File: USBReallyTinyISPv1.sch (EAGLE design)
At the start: 20 parts, among them IC1 ATTINY2313, IC2 74AC125D, Q1 12 MHz, X1 miniUSB-B

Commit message: Getting it ready for printing
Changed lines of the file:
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@@
 <?xml version="1.0" encoding="utf-8"?>
 <!DOCTYPE eagle SYSTEM "eagle.dtd">
-<eagle version="6.1">
+<eagle version="7.4.0">
 <drawing>
 <settings>
@@
 <segment>
 <pinref part="IC1" gate="G$1" pin="(T0)PD4"/>
-<wire x1="99.06" y1="71.12" x2="116.84" y2="71.12" width="0.1524" layer="91"/>
-<wire x1="116.84" y1="71.12" x2="116.84" y2="119.38" width="0.1524" layer="91"/>
+<wire x1="99.06" y1="71.12" x2="114.3" y2="71.12" width="0.1524" layer="91"/>
+<wire x1="114.3" y1="71.12" x2="114.3" y2="119.38" width="0.1524" layer="91"/>
 <pinref part="IC2" gate="D" pin="OE"/>
-<wire x1="116.84" y1="119.38" x2="101.6" y2="119.38" width="0.1524" layer="91"/>
+<wire x1="114.3" y1="119.38" x2="101.6" y2="119.38" width="0.1524" layer="91"/>
 <pinref part="IC2" gate="C" pin="OE"/>
-<wire x1="116.84" y1="119.38" x2="134.62" y2="119.38" width="0.1524" layer="91"/>
+<wire x1="114.3" y1="119.38" x2="134.62" y2="119.38" width="0.1524" layer="91"/>
 <wire x1="134.62" y1="119.38" x2="134.62" y2="121.92" width="0.1524" layer="91"/>
 <pinref part="IC2" gate="B" pin="OE"/>
@@
 <junction x="134.62" y="121.92"/>
 <junction x="134.62" y="139.7"/>
-<junction x="116.84" y="119.38"/>
-</segment>
-</net>
+<junction x="114.3" y="119.38"/>
+</segment>
+</net>

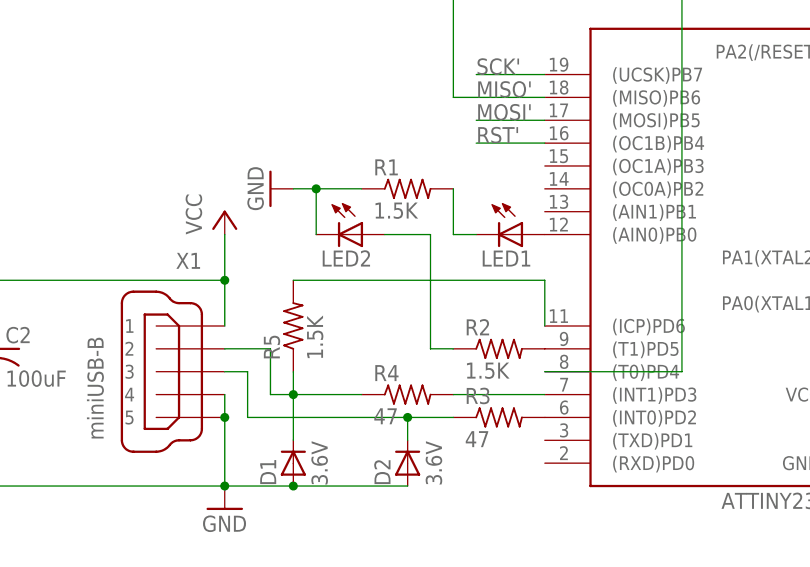
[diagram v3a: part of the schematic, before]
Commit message: Changed size of 1.5kOhm resistors
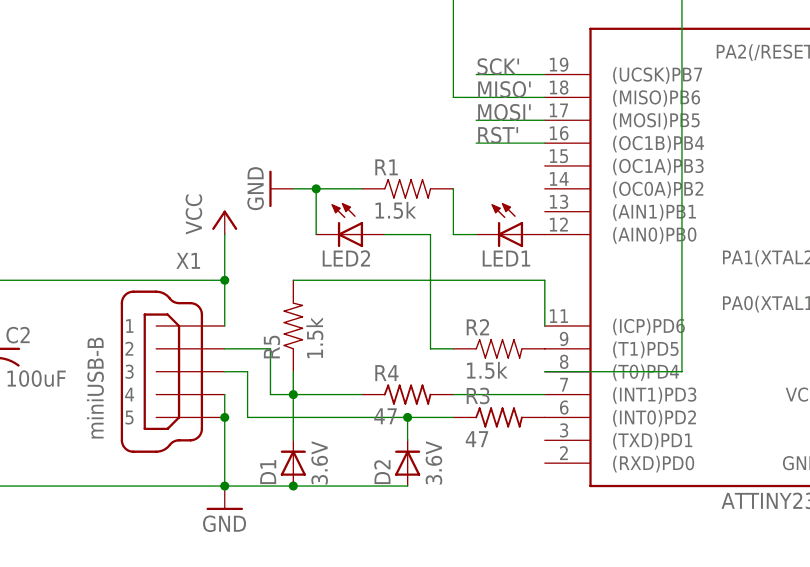
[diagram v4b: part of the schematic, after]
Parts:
- R1, R2, R5: value 1.5K -> 1.5k; device resistor:R-US_R0805 -> SparkFun-Resistors:RESISTOR1206
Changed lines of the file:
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@@
 <layer number="223" name="223bmp" color="24" fill="1" visible="no" active="no"/>
 <layer number="224" name="224bmp" color="25" fill="1" visible="no" active="no"/>
+<layer number="225" name="225bmp" color="7" fill="1" visible="yes" active="yes"/>
+<layer number="226" name="226bmp" color="7" fill="1" visible="yes" active="yes"/>
+<layer number="227" name="227bmp" color="7" fill="1" visible="yes" active="yes"/>
+<layer number="228" name="228bmp" color="7" fill="1" visible="yes" active="yes"/>
+<layer number="229" name="229bmp" color="7" fill="1" visible="yes" active="yes"/>
+<layer number="230" name="230bmp" color="7" fill="1" visible="yes" active="yes"/>
 <layer number="231" name="Eagle3D_PG1" color="7" fill="1" visible="no" active="no"/>
 <layer number="232" name="Eagle3D_PG2" color="7" fill="1" visible="no" active="no"/>
@@
 <part name="IC2" library="74xx-eu" deviceset="74*125" device="D" technology="AC"/>
 <part name="Q1" library="murata-filter" deviceset="CSTCR" device="" technology="6M00G53Z" value="12 MHz"/>
-<part name="R1" library="resistor" deviceset="R-US_" device="R0805" value="1.5K"/>
-<part name="R2" library="resistor" deviceset="R-US_" device="R0805" value="1.5K"/>
 <part name="R3" library="resistor" deviceset="R-US_" device="R0805" value="47"/>
 <part name="R4" library="resistor" deviceset="R-US_" device="R0805" value="47"/>
-<part name="R5" library="resistor" deviceset="R-US_" device="R0805" value="1.5K"/>
 <part name="R6" library="resistor" deviceset="R-US_" device="R0805" value="10K"/>
 <part name="IC1" library="avr-7" deviceset="TINY2313*" device="-*S*" value="ATTINY2313"/>
@@
 <part name="GND5" library="supply1" deviceset="GND" device=""/>
 <part name="JP1" library="adafruit" deviceset="PINHD-1X3" device=""/>
+<part name="R1" library="SparkFun-Resistors" deviceset="RESISTOR" device="1206" value="1.5k"/>
+<part name="R2" library="SparkFun-Resistors" deviceset="RESISTOR" device="1206" value="1.5k"/>
+<part name="R5" library="SparkFun-Resistors" deviceset="RESISTOR" device="1206" value="1.5k"/>
 </parts>
 <sheets>
@@
 </instance>
 <instance part="Q1" gate="G$1" x="144.78" y="81.28" rot="R90"/>
-<instance part="R1" gate="G$1" x="83.82" y="91.44"/>
-<instance part="R2" gate="G$1" x="93.98" y="73.66"/>
 <instance part="R3" gate="G$1" x="93.98" y="66.04"/>
 <instance part="R4" gate="G$1" x="83.82" y="68.58"/>
-<instance part="R5" gate="G$1" x="71.12" y="76.2" rot="R90"/>
 <instance part="R6" gate="G$1" x="142.24" y="106.68"/>
 <instance part="IC1" gate="G$1" x="116.84" y="88.9" rot="MR0"/>
@@
 <instance part="GND5" gate="1" x="71.12" y="134.62"/>
 <instance part="JP1" gate="A" x="81.28" y="152.4" rot="R90"/>
+<instance part="R1" gate="G$1" x="83.82" y="91.44"/>
+<instance part="R2" gate="G$1" x="93.98" y="73.66"/>
+<instance part="R5" gate="G$1" x="71.12" y="76.2" rot="R90"/>
 </instances>
 <busses>
@@
 </segment>
 <segment>
-<pinref part="R1" gate="G$1" pin="1"/>
 <pinref part="GND3" gate="1" pin="GND"/>
 <wire x1="78.74" y1="91.44" x2="73.66" y2="91.44" width="0.1524" layer="91"/>
@@
 <wire x1="73.66" y1="86.36" x2="73.66" y2="91.44" width="0.1524" layer="91"/>
 <junction x="73.66" y="91.44"/>
+<pinref part="R1" gate="G$1" pin="1"/>
 </segment>
 <segment>
@@
 </segment>
 </net>
-<net name="N$5" class="0">
-<segment>
-<pinref part="IC1" gate="G$1" pin="(T1)PD5"/>
-<pinref part="R2" gate="G$1" pin="2"/>
-</segment>
-</net>
 <net name="N$6" class="0">
 <segment>
 <wire x1="81.28" y1="86.36" x2="86.36" y2="86.36" width="0.1524" layer="91"/>
 <wire x1="86.36" y1="86.36" x2="86.36" y2="73.66" width="0.1524" layer="91"/>
-<pinref part="R2" gate="G$1" pin="1"/>
 <wire x1="86.36" y1="73.66" x2="88.9" y2="73.66" width="0.1524" layer="91"/>
 <pinref part="LED2" gate="G$1" pin="A"/>
+<pinref part="R2" gate="G$1" pin="1"/>
 </segment>
 </net>
 <net name="N$7" class="0">
 <segment>
-<pinref part="R1" gate="G$1" pin="2"/>
 <wire x1="88.9" y1="86.36" x2="88.9" y2="91.44" width="0.1524" layer="91"/>
 <pinref part="LED1" gate="G$1" pin="C"/>
 <wire x1="91.44" y1="86.36" x2="88.9" y2="86.36" width="0.1524" layer="91"/>
+<pinref part="R1" gate="G$1" pin="2"/>
 </segment>
 </net>
@@
 <wire x1="71.12" y1="63.5" x2="71.12" y2="68.58" width="0.1524" layer="91"/>
 <junction x="71.12" y="68.58"/>
-<pinref part="R5" gate="G$1" pin="1"/>
 <wire x1="71.12" y1="68.58" x2="71.12" y2="71.12" width="0.1524" layer="91"/>
 <pinref part="D1" gate="G$1" pin="K"/>
+<pinref part="R5" gate="G$1" pin="1"/>
 </segment>
 </net>
@@
 <segment>
 <pinref part="IC1" gate="G$1" pin="(ICP)PD6"/>
-<pinref part="R5" gate="G$1" pin="2"/>
 <wire x1="99.06" y1="76.2" x2="99.06" y2="81.28" width="0.1524" layer="91"/>
 <wire x1="99.06" y1="81.28" x2="71.12" y2="81.28" width="0.1524" layer="91"/>
+<pinref part="R5" gate="G$1" pin="2"/>
 </segment>
 </net>
@@
 </segment>
 </net>
+<net name="N$5" class="0">
+<segment>
+<pinref part="IC1" gate="G$1" pin="(T1)PD5"/>
+<pinref part="R2" gate="G$1" pin="2"/>
+</segment>
+</net>

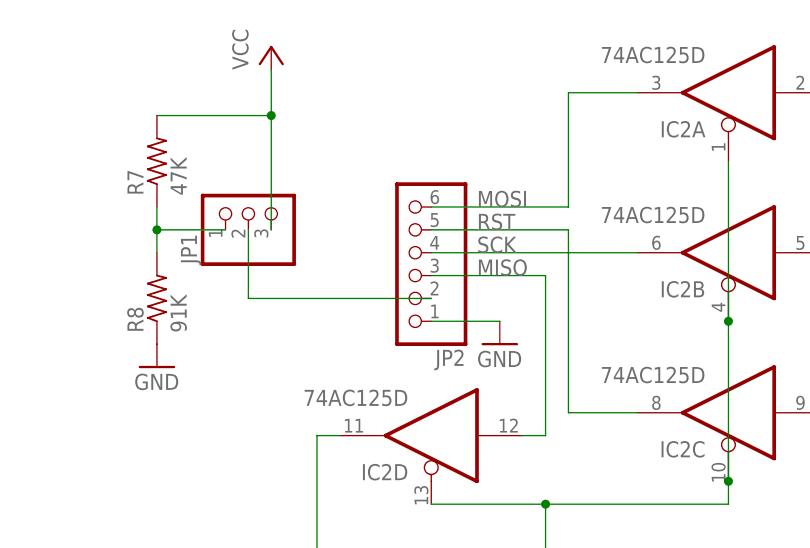
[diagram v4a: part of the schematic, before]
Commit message: Updated headers to have bigger pads
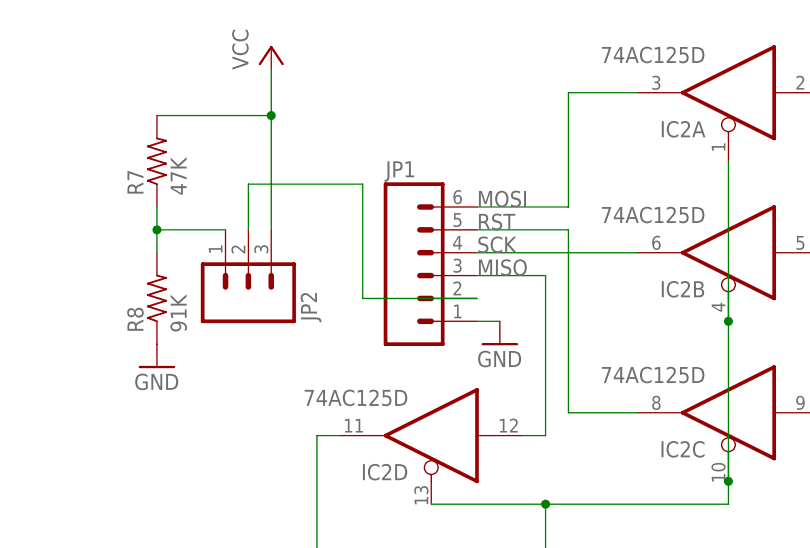
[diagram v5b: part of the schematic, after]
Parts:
- JP1: device adafruit:PINHD-1X3 -> SparkFun-Connectors:M06SILK_FEMALE_PTH
- JP2: device adafruit:PINHD-1X6 -> mine:M03-SHORTEDPTH
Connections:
- net GND: now also JP1.1; no longer JP2.1
- net MISO: now also JP1.3; no longer JP2.3
- net MOSI: now also JP1.6; no longer JP2.6
- net N$15: now also JP2.1; no longer JP1.1
- net RST: now also JP1.5; no longer JP2.5
- net SCK: now also JP1.4; no longer JP2.4
- net VCC: now also JP2.3; no longer JP1.3
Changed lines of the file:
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@@
 <?xml version="1.0" encoding="utf-8"?>
 <!DOCTYPE eagle SYSTEM "eagle.dtd">
-<eagle version="7.4.0">
+<eagle version="6.6.0">
 <drawing>
 <settings>
@@
 <layer number="56" name="wert" color="7" fill="1" visible="no" active="no"/>
 <layer number="57" name="tCAD" color="7" fill="1" visible="no" active="no"/>
+<layer number="59" name="tCarbon" color="7" fill="1" visible="no" active="no"/>
+<layer number="60" name="bCarbon" color="7" fill="1" visible="no" active="no"/>
 <layer number="90" name="Modules" color="7" fill="1" visible="no" active="yes"/>
 <layer number="91" name="Nets" color="2" fill="1" visible="yes" active="yes"/>
@@
 <layer number="112" name="tSilk" color="7" fill="1" visible="yes" active="yes"/>
 <layer number="113" name="ReferenceLS" color="7" fill="1" visible="no" active="no"/>
+<layer number="114" name="Badge_Outline" color="7" fill="1" visible="yes" active="yes"/>
+<layer number="115" name="ReferenceISLANDS" color="7" fill="1" visible="yes" active="yes"/>
 <layer number="116" name="Patch_BOT" color="9" fill="4" visible="yes" active="yes"/>
 <layer number="118" name="Rect_Pads" color="7" fill="1" visible="no" active="no"/>
@@
 <layer number="127" name="_tValues" color="7" fill="1" visible="yes" active="yes"/>
 <layer number="128" name="_bValues" color="7" fill="1" visible="yes" active="yes"/>
+<layer number="129" name="Mask" color="7" fill="1" visible="yes" active="yes"/>
 <layer number="131" name="tAdjust" color="7" fill="1" visible="no" active="yes"/>
 <layer number="132" name="bAdjust" color="7" fill="1" visible="no" active="yes"/>
@@
 <layer number="251" name="SMDround" color="7" fill="1" visible="no" active="no"/>
 <layer number="254" name="cooling" color="7" fill="1" visible="yes" active="yes"/>
+<layer number="255" name="routoute" color="7" fill="1" visible="yes" active="yes"/>
 </layers>
 <schematic xreflabel="%F%N/%S.%C%R" xrefpart="/%S.%C%R">
@@
 <part name="D1" library="ipc-7351-diode" deviceset="DIODE_" device="SOD-123" value="3.6V"/>
 <part name="D2" library="ipc-7351-diode" deviceset="DIODE_" device="SOD-123" value="3.6V"/>
-<part name="JP2" library="adafruit" deviceset="PINHD-1X6" device=""/>
 <part name="GND6" library="supply1" deviceset="GND" device=""/>
 <part name="R7" library="resistor" deviceset="R-US_" device="R0805" value="47K"/>
 <part name="R8" library="resistor" deviceset="R-US_" device="R0805" value="91K"/>
 <part name="GND5" library="supply1" deviceset="GND" device=""/>
-<part name="JP1" library="adafruit" deviceset="PINHD-1X3" device=""/>
 <part name="R1" library="SparkFun-Resistors" deviceset="RESISTOR" device="1206" value="1.5k"/>
 <part name="R2" library="SparkFun-Resistors" deviceset="RESISTOR" device="1206" value="1.5k"/>
 <part name="R5" library="SparkFun-Resistors" deviceset="RESISTOR" device="1206" value="1.5k"/>
+<part name="JP1" library="SparkFun-Connectors" deviceset="M06" device="SILK_FEMALE_PTH"/>
+<part name="JP2" library="mine" deviceset="M03-SHORTED" device="PTH"/>
 </parts>
 <sheets>
@@
 <instance part="D1" gate="G$1" x="71.12" y="60.96" rot="R90"/>
 <instance part="D2" gate="G$1" x="83.82" y="60.96" rot="R90"/>
-<instance part="JP2" gate="A" x="99.06" y="147.32" rot="R180"/>
 <instance part="GND6" gate="1" x="109.22" y="137.16"/>
 <instance part="R7" gate="G$1" x="71.12" y="157.48" rot="R90"/>
 <instance part="R8" gate="G$1" x="71.12" y="142.24" rot="R90"/>
 <instance part="GND5" gate="1" x="71.12" y="134.62"/>
-<instance part="JP1" gate="A" x="81.28" y="152.4" rot="R90"/>
 <instance part="R1" gate="G$1" x="83.82" y="91.44"/>
 <instance part="R2" gate="G$1" x="93.98" y="73.66"/>
 <instance part="R5" gate="G$1" x="71.12" y="76.2" rot="R90"/>
+<instance part="JP1" gate="G$1" x="101.6" y="144.78"/>
+<instance part="JP2" gate="G$1" x="81.28" y="142.24" rot="MR90"/>
 </instances>
 <busses>
@@
 </segment>
 <segment>
-<pinref part="JP2" gate="A" pin="1"/>
 <pinref part="GND6" gate="1" pin="GND"/>
-<wire x1="101.6" y1="139.7" x2="109.22" y2="139.7" width="0.1524" layer="91"/>
+<wire x1="106.68" y1="139.7" x2="109.22" y2="139.7" width="0.1524" layer="91"/>
+<pinref part="JP1" gate="G$1" pin="1"/>
 </segment>
 <segment>
@@
 <wire x1="71.12" y1="162.56" x2="83.82" y2="162.56" width="0.1524" layer="91"/>
 <junction x="83.82" y="162.56"/>
-<pinref part="JP1" gate="A" pin="3"/>
+<pinref part="JP2" gate="G$1" pin="3"/>
 </segment>
 </net>
@@
 <pinref part="IC2" gate="A" pin="O"/>
 <wire x1="124.46" y1="165.1" x2="116.84" y2="165.1" width="0.1524" layer="91"/>
-<pinref part="JP2" gate="A" pin="6"/>
-<wire x1="101.6" y1="152.4" x2="116.84" y2="152.4" width="0.1524" layer="91"/>
+<wire x1="106.68" y1="152.4" x2="116.84" y2="152.4" width="0.1524" layer="91"/>
 <wire x1="116.84" y1="152.4" x2="116.84" y2="165.1" width="0.1524" layer="91"/>
+<pinref part="JP1" gate="G$1" pin="6"/>
 </segment>
 </net>
@@
 <label x="106.68" y="144.78" size="1.778" layer="95"/>
 <pinref part="IC2" gate="D" pin="I"/>
-<pinref part="JP2" gate="A" pin="3"/>
 <wire x1="114.3" y1="144.78" x2="114.3" y2="127" width="0.1524" layer="91"/>
 <wire x1="114.3" y1="127" x2="111.76" y2="127" width="0.1524" layer="91"/>
-<wire x1="101.6" y1="144.78" x2="114.3" y2="144.78" width="0.1524" layer="91"/>
+<wire x1="106.68" y1="144.78" x2="114.3" y2="144.78" width="0.1524" layer="91"/>
+<pinref part="JP1" gate="G$1" pin="3"/>
 </segment>
 </net>
@@
 <label x="106.68" y="147.32" size="1.778" layer="95"/>
 <pinref part="IC2" gate="B" pin="O"/>
-<wire x1="124.46" y1="147.32" x2="101.6" y2="147.32" width="0.1524" layer="91"/>
-<pinref part="JP2" gate="A" pin="4"/>
+<wire x1="124.46" y1="147.32" x2="106.68" y2="147.32" width="0.1524" layer="91"/>
+<pinref part="JP1" gate="G$1" pin="4"/>
 </segment>
 </net>
@@
 <wire x1="116.84" y1="149.86" x2="116.84" y2="129.54" width="0.1524" layer="91"/>
 <wire x1="116.84" y1="129.54" x2="124.46" y2="129.54" width="0.1524" layer="91"/>
-<pinref part="JP2" gate="A" pin="5"/>
-<wire x1="101.6" y1="149.86" x2="116.84" y2="149.86" width="0.1524" layer="91"/>
+<wire x1="106.68" y1="149.86" x2="116.84" y2="149.86" width="0.1524" layer="91"/>
+<pinref part="JP1" gate="G$1" pin="5"/>
 </segment>
 </net>
@@
 <net name="N$13" class="0">
 <segment>
-<pinref part="JP2" gate="A" pin="2"/>
-<wire x1="101.6" y1="142.24" x2="81.28" y2="142.24" width="0.1524" layer="91"/>
-<wire x1="81.28" y1="142.24" x2="81.28" y2="149.86" width="0.1524" layer="91"/>
-<pinref part="JP1" gate="A" pin="2"/>
+<wire x1="81.28" y1="149.86" x2="81.28" y2="154.94" width="0.1524" layer="91"/>
+<wire x1="81.28" y1="154.94" x2="93.98" y2="154.94" width="0.1524" layer="91"/>
+<pinref part="JP1" gate="G$1" pin="2"/>
+<wire x1="106.68" y1="142.24" x2="93.98" y2="142.24" width="0.1524" layer="91"/>
+<wire x1="93.98" y1="142.24" x2="93.98" y2="154.94" width="0.1524" layer="91"/>
+<pinref part="JP2" gate="G$1" pin="2"/>
 </segment>
 </net>
@@
 <wire x1="78.74" y1="149.86" x2="71.12" y2="149.86" width="0.1524" layer="91"/>
 <junction x="71.12" y="149.86"/>
-<pinref part="JP1" gate="A" pin="1"/>
-</segment>
-</net>
+<pinref part="JP2" gate="G$1" pin="1"/>
+</segment>
+</net>
